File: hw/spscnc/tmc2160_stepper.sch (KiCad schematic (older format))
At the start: 65 parts, among them IC1 TMC2160-TA, Q13 KIA50N06B, Q14 KIA50N06B, Q15 KIA50N06B, Q5 KIA50N06B, Q6 KIA50N06B, Q7 KIA50N06B, Q8 KIA50N06B, Q9 KIA50N06B

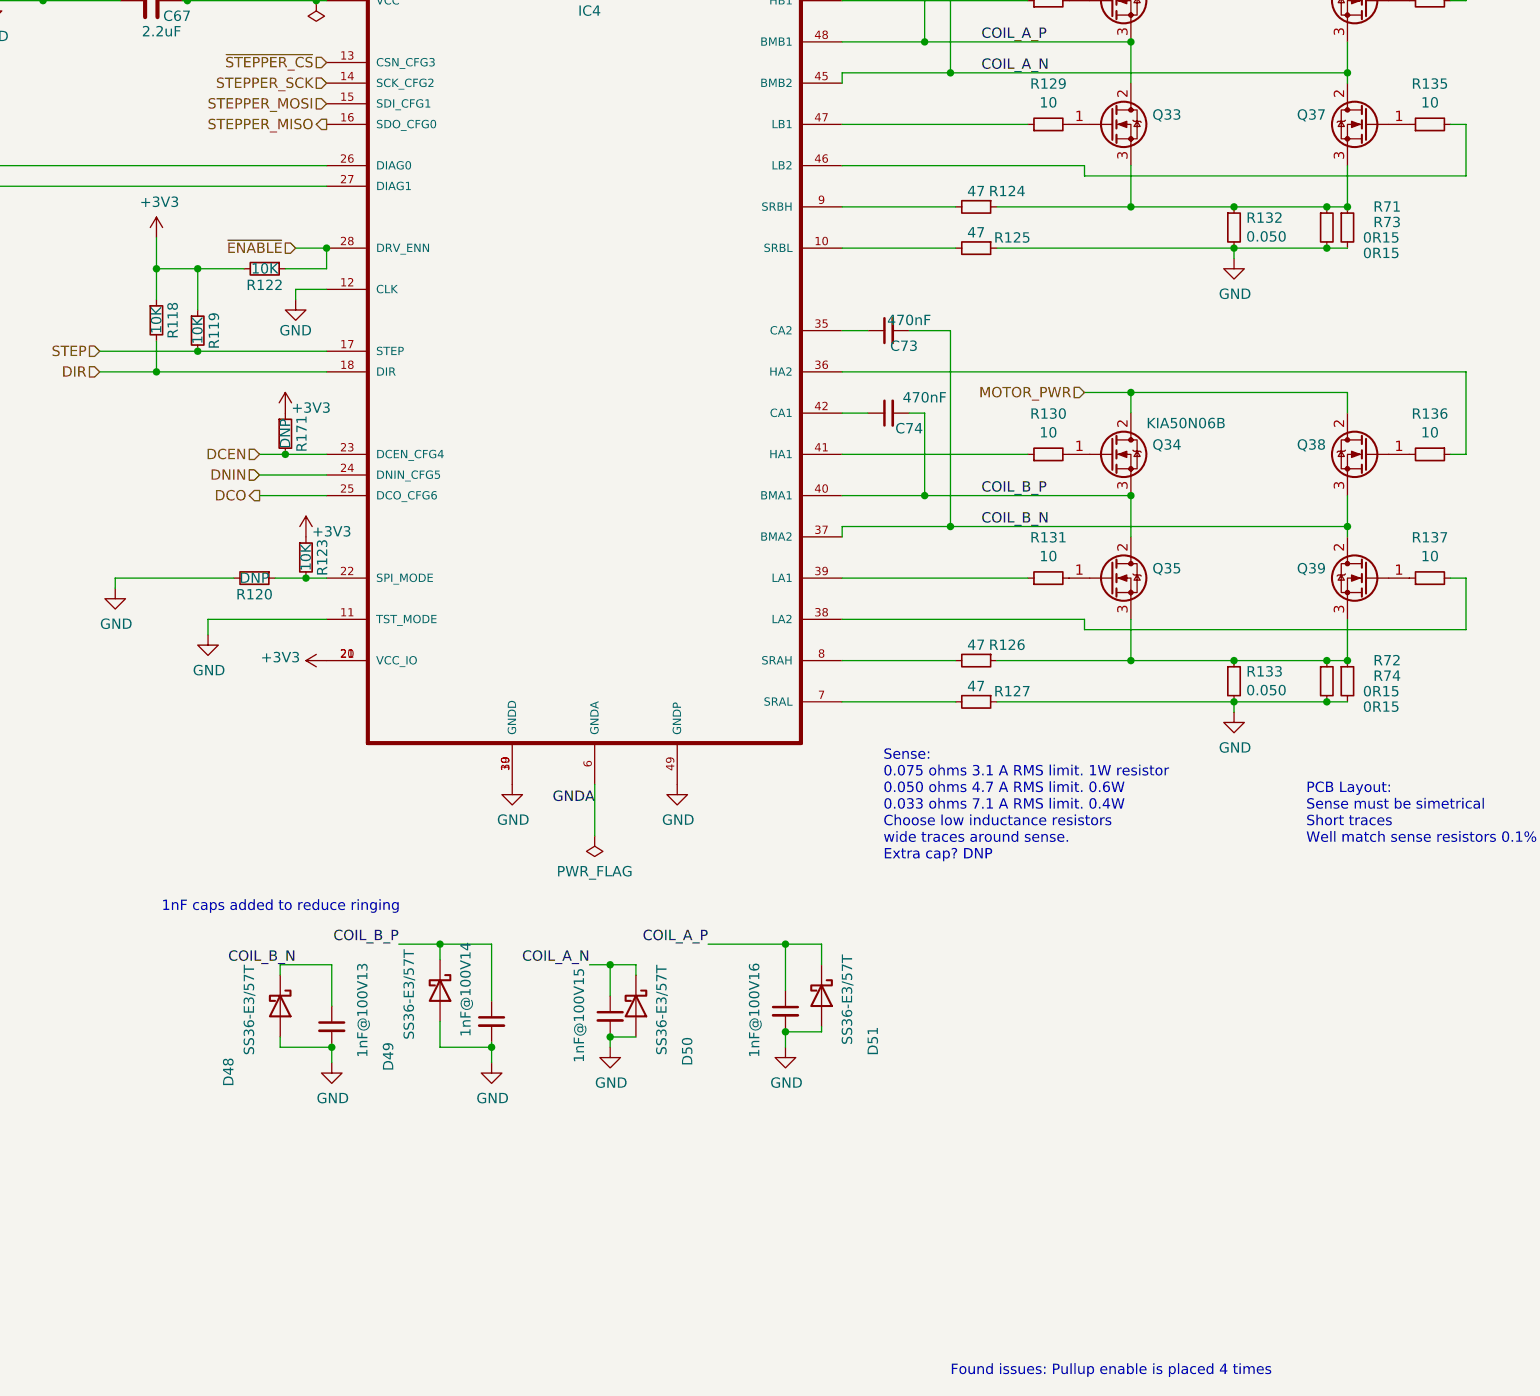
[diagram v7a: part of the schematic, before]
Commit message: Revision 1.1.0 With only critical corrections. Pending some work on the relays as that part could be remade from scratch for flexibility.
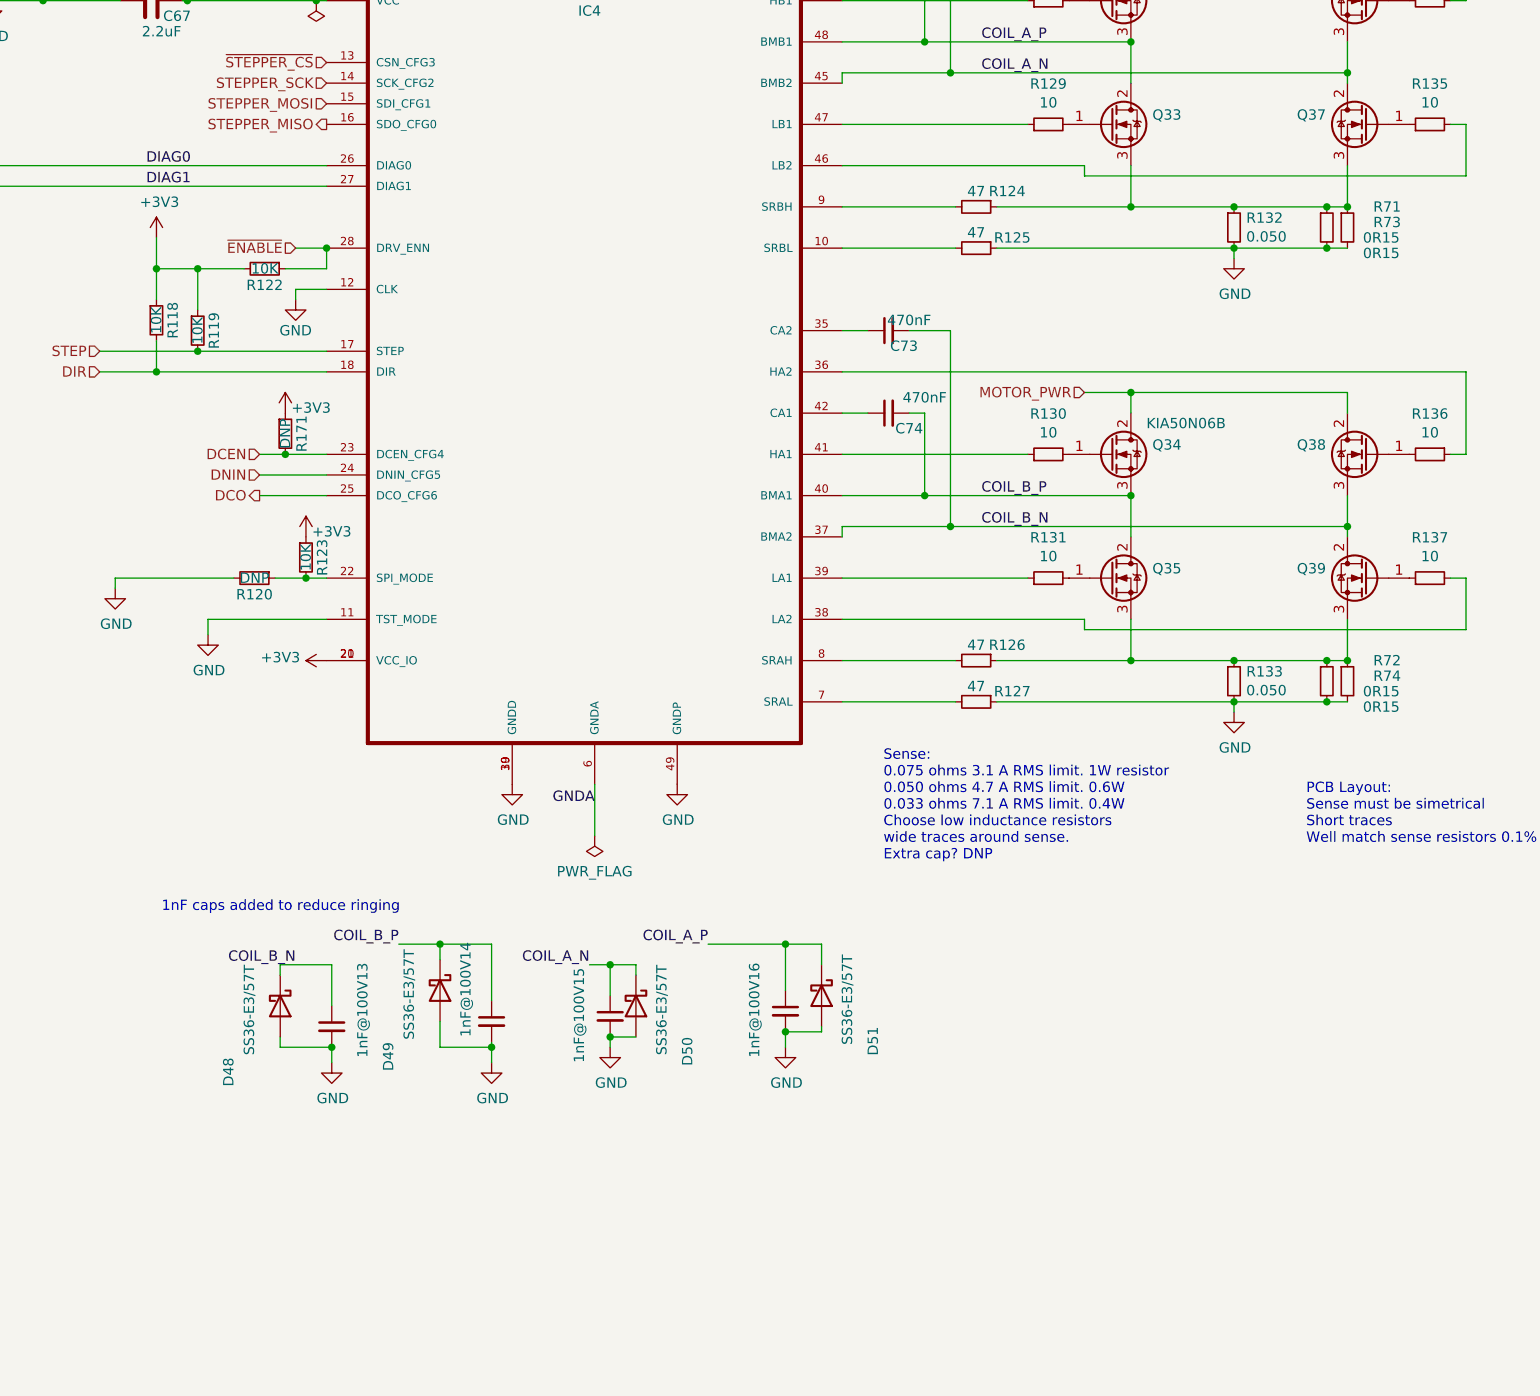
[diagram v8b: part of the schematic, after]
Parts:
- H3, H4: footprint MountingHole:MountingHole_2.2mm_M2_Pad_Via -> MountingHole:MountingHole_3.2mm_M3_Pad_Via
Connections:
- net DIAG0: now reaches D3.1 (K), IC1.26 (DIAG0)
- net DIAG1: now reaches D2.1 (K), IC1.27 (DIAG1)
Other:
- note removed: "Found issues: Pullup enable is placed 4 times"
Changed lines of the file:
@@
 Sheet 12 17
 Title "Trinamic FluidNC CNC Controller"
-Date "2022-02-12"
-Rev "1.0.1"
+Date "2022-04-29"
+Rev "1.1.0"
 Comp ""
 Comment1 ""
@@
 AR Path="/61E6E495" Ref="#PWR0103"  Part="1"
 AR Path="/6221509B/61E6E495" Ref="#PWR?"  Part="1"
-F 0 "#PWR085" H 1875 1825 50  0001 C CNN
+F 0 "#PWR065" H 1875 1825 50  0001 C CNN
 F 1 "GND" H 1880 1902 50  0000 C CNN
 F 2 "" H 1875 2075 50  0001 C CNN
@@
 AR Path="/61E77854" Ref="#PWR0104"  Part="1"
 AR Path="/6221509B/61E77854" Ref="#PWR?"  Part="1"
-F 0 "#PWR096" H 7050 800 50  0001 C CNN
+F 0 "#PWR076" H 7050 800 50  0001 C CNN
 F 1 "GND" H 7055 877 50  0000 C CNN
 F 2 "" H 7050 1050 50  0001 C CNN
@@
 AR Path="/61E77EC9" Ref="#PWR0105"  Part="1"
 AR Path="/6221509B/61E77EC9" Ref="#PWR?"  Part="1"
-F 0 "#PWR0100" H 8525 800 50  0001 C CNN
+F 0 "#PWR080" H 8525 800 50  0001 C CNN
 F 1 "GND" H 8530 877 50  0000 C CNN
 F 2 "" H 8525 1050 50  0001 C CNN
@@
 AR Path="/6203DFCF/61E7935F" Ref="#PWR091"  Part="1"
 AR Path="/6221509B/61E7935F" Ref="#PWR?"  Part="1"
-F 0 "#PWR091" H 3500 5125 50  0001 C CNN
+F 0 "#PWR071" H 3500 5125 50  0001 C CNN
 F 1 "+3V3" V 3515 5403 50  0000 L CNN
 F 2 "" H 3500 5275 50  0001 C CNN
@@
 AR Path="/61E79E80" Ref="#PWR0110"  Part="1"
 AR Path="/6221509B/61E79E80" Ref="#PWR?"  Part="1"
-F 0 "#PWR084" H 1875 1325 50  0001 C CNN
+F 0 "#PWR064" H 1875 1325 50  0001 C CNN
 F 1 "+12V" H 1890 1648 50  0000 C CNN
 F 2 "" H 1875 1475 50  0001 C CNN
@@
 AR Path="/61E86B21" Ref="#PWR0115"  Part="1"
 AR Path="/6221509B/61E86B21" Ref="#PWR?"  Part="1"
-F 0 "#PWR092" H 4400 5625 50  0001 C CNN
+F 0 "#PWR072" H 4400 5625 50  0001 C CNN
 F 1 "GND" H 4405 5702 50  0000 C CNN
 F 2 "" H 4400 5875 50  0001 C CNN
@@
 AR Path="/61E86EEA" Ref="#PWR0116"  Part="1"
 AR Path="/6221509B/61E86EEA" Ref="#PWR?"  Part="1"
-F 0 "#PWR094" H 5200 5625 50  0001 C CNN
+F 0 "#PWR074" H 5200 5625 50  0001 C CNN
 F 1 "GND" H 5205 5702 50  0000 C CNN
 F 2 "" H 5200 5875 50  0001 C CNN
@@
 AR Path="/6203DFCF/61E89FDE" Ref="#PWR087"  Part="1"
 AR Path="/6221509B/61E89FDE" Ref="#PWR?"  Part="1"
-F 0 "#PWR087" H 2675 3075 50  0001 C CNN
+F 0 "#PWR067" H 2675 3075 50  0001 C CNN
 F 1 "+3V3" H 2690 3398 50  0000 C CNN
 F 2 "" H 2675 3225 50  0001 C CNN
@@
 AR Path="/6203DFCF/61E8CEFE" Ref="#PWR089"  Part="1"
 AR Path="/6221509B/61E8CEFE" Ref="#PWR?"  Part="1"
-F 0 "#PWR089" H 3350 3275 50  0001 C CNN
+F 0 "#PWR069" H 3350 3275 50  0001 C CNN
 F 1 "GND" H 3350 3375 50  0000 C CNN
 F 2 "" H 3350 3525 50  0001 C CNN
@@
 AR Path="/6203DFCF/61EA6B53" Ref="#PWR090"  Part="1"
 AR Path="/6221509B/61EA6B53" Ref="#PWR?"  Part="1"
-F 0 "#PWR090" H 3400 4525 50  0001 C CNN
+F 0 "#PWR070" H 3400 4525 50  0001 C CNN
 F 1 "+3V3" H 3525 4700 50  0000 C CNN
 F 2 "" H 3400 4675 50  0001 C CNN
@@
 AR Path="/61ECB3CC" Ref="#PWR0121"  Part="1"
 AR Path="/6221509B/61ECB3CC" Ref="#PWR?"  Part="1"
-F 0 "#PWR099" H 8075 800 50  0001 C CNN
+F 0 "#PWR079" H 8075 800 50  0001 C CNN
 F 1 "GND" H 8080 877 50  0000 C CNN
 F 2 "" H 8075 1050 50  0001 C CNN
@@
 AR Path="/61F1EBF7" Ref="#PWR0122"  Part="1"
 AR Path="/6221509B/61F1EBF7" Ref="#PWR?"  Part="1"
-F 0 "#PWR097" H 7900 3075 50  0001 C CNN
+F 0 "#PWR077" H 7900 3075 50  0001 C CNN
 F 1 "GND" H 7905 3152 50  0000 C CNN
 F 2 "" H 7900 3325 50  0001 C CNN
@@
 AR Path="/61F26F6F" Ref="#PWR0123"  Part="1"
 AR Path="/6221509B/61F26F6F" Ref="#PWR?"  Part="1"
-F 0 "#PWR088" H 2925 4900 50  0001 C CNN
+F 0 "#PWR068" H 2925 4900 50  0001 C CNN
 F 1 "GND" H 2930 4977 50  0000 C CNN
 F 2 "" H 2925 5150 50  0001 C CNN
@@
 AR Path="/61F3F591" Ref="#PWR0124"  Part="1"
 AR Path="/6221509B/61F3F591" Ref="#PWR?"  Part="1"
-F 0 "#PWR086" H 2475 4675 50  0001 C CNN
+F 0 "#PWR066" H 2475 4675 50  0001 C CNN
 F 1 "GND" H 2480 4752 50  0000 C CNN
 F 2 "" H 2475 4925 50  0001 C CNN
@@
 F 0 "H7" H 10575 5674 50  0000 L CNN
 F 1 "MountingHole_Pad" H 10575 5583 50  0001 L CNN
-F 2 "MountingHole:MountingHole_2.2mm_M2_Pad_Via" H 10475 5625 50  0001 C CNN
+F 2 "MountingHole:MountingHole_3.2mm_M3_Pad_Via" H 10475 5625 50  0001 C CNN
 F 3 "~" H 10475 5625 50  0001 C CNN
 F 4 "DNP003" H 10475 5625 50  0001 C CNN "jlcpcb"
@@
 AR Path="/61F4F366" Ref="#PWR0125"  Part="1"
 AR Path="/6221509B/61F4F366" Ref="#PWR?"  Part="1"
-F 0 "#PWR095" H 10475 5475 50  0001 C CNN
+F 0 "#PWR075" H 10475 5475 50  0001 C CNN
 F 1 "GND" H 10480 5552 50  0000 C CNN
 F 2 "" H 10475 5725 50  0001 C CNN
@@
 AR Path="/61F62E48" Ref="#PWR0126"  Part="1"
 AR Path="/6221509B/61F62E48" Ref="#PWR?"  Part="1"
-F 0 "#PWR0120" H 9075 800 50  0001 C CNN
+F 0 "#PWR081" H 9075 800 50  0001 C CNN
 F 1 "GND" H 9080 877 50  0000 C CNN
 F 2 "" H 9075 1050 50  0001 C CNN
@@
 AR Path="/61F7F4E7" Ref="#PWR0127"  Part="1"
 AR Path="/6221509B/61F7F4E7" Ref="#PWR?"  Part="1"
-F 0 "#PWR098" H 7900 5275 50  0001 C CNN
+F 0 "#PWR078" H 7900 5275 50  0001 C CNN
 F 1 "GND" H 7905 5352 50  0000 C CNN
 F 2 "" H 7900 5525 50  0001 C CNN
@@
 AR Path="/620590A8" Ref="#FLG0110"  Part="1"
 AR Path="/6221509B/620590A8" Ref="#FLG?"  Part="1"
-F 0 "#FLG0113" H 3450 2150 50  0001 C CNN
+F 0 "#FLG0112" H 3450 2150 50  0001 C CNN
 F 1 "PWR_FLAG" H 3450 2248 50  0001 C CNN
 F 2 "" H 3450 2075 50  0001 C CNN
@@
 F 0 "H10" H 10225 5674 50  0000 L CNN
 F 1 "MountingHole_Pad" H 10225 5583 50  0001 L CNN
-F 2 "MountingHole:MountingHole_2.2mm_M2_Pad_Via" H 10125 5625 50  0001 C CNN
+F 2 "MountingHole:MountingHole_3.2mm_M3_Pad_Via" H 10125 5625 50  0001 C CNN
 F 3 "~" H 10125 5625 50  0001 C CNN
 F 4 "DNP003" H 10125 5625 50  0001 C CNN "jlcpcb"
@@
 AR Path="/61FC2A3D" Ref="#PWR03"  Part="1"
 AR Path="/6221509B/61FC2A3D" Ref="#PWR?"  Part="1"
-F 0 "#PWR037" H 10125 5475 50  0001 C CNN
+F 0 "#PWR06" H 10125 5475 50  0001 C CNN
 F 1 "GND" H 10130 5552 50  0000 C CNN
 F 2 "" H 10125 5725 50  0001 C CNN
@@
 AR Path="/6203DFCF/61F301A3" Ref="#PWR0239"  Part="1"
 AR Path="/6221509B/61F301A3" Ref="#PWR?"  Part="1"
-F 0 "#PWR0239" H 3300 3925 50  0001 C CNN
+F 0 "#PWR0238" H 3300 3925 50  0001 C CNN
 F 1 "+3V3" H 3425 4100 50  0000 C CNN
 F 2 "" H 3300 4075 50  0001 C CNN
@@
 AR Path="/6203DFCF/61F599E0" Ref="#PWR0244"  Part="1"
 AR Path="/6221509B/61F599E0" Ref="#PWR?"  Part="1"
-F 0 "#PWR0244" H 1425 2125 50  0001 C CNN
+F 0 "#PWR0242" H 1425 2125 50  0001 C CNN
 F 1 "+3V3" H 1440 2448 50  0000 C CNN
 F 2 "" H 1425 2275 50  0001 C CNN
@@
 AR Path="/6203DFCF/61F5A3EC" Ref="#PWR0245"  Part="1"
 AR Path="/6221509B/61F5A3EC" Ref="#PWR?"  Part="1"
-F 0 "#PWR0245" H 1050 2200 50  0001 C CNN
+F 0 "#PWR0243" H 1050 2200 50  0001 C CNN
 F 1 "+3V3" H 1065 2523 50  0000 C CNN
 F 2 "" H 1050 2350 50  0001 C CNN
@@
 AR Path="/61FAA995" Ref="#PWR0247"  Part="1"
 AR Path="/6221509B/61FAA995" Ref="#PWR?"  Part="1"
-F 0 "#PWR0259" H 3525 6975 50  0001 C CNN
+F 0 "#PWR0255" H 3525 6975 50  0001 C CNN
 F 1 "GND" H 3530 7052 50  0000 C CNN
 F 2 "" H 3525 7225 50  0001 C CNN
@@
 AR Path="/61FAED05" Ref="#PWR0248"  Part="1"
 AR Path="/6221509B/61FAED05" Ref="#PWR?"  Part="1"
-F 0 "#PWR0260" H 4300 6975 50  0001 C CNN
+F 0 "#PWR0256" H 4300 6975 50  0001 C CNN
 F 1 "GND" H 4305 7052 50  0000 C CNN
 F 2 "" H 4300 7225 50  0001 C CNN
@@
 AR Path="/61FB6882" Ref="#PWR0249"  Part="1"
 AR Path="/6221509B/61FB6882" Ref="#PWR?"  Part="1"
-F 0 "#PWR0261" H 4875 6900 50  0001 C CNN
+F 0 "#PWR0257" H 4875 6900 50  0001 C CNN
 F 1 "GND" H 4880 6977 50  0000 C CNN
 F 2 "" H 4875 7150 50  0001 C CNN
@@
 AR Path="/61FBE4C1" Ref="#PWR0250"  Part="1"
 AR Path="/6221509B/61FBE4C1" Ref="#PWR?"  Part="1"
-F 0 "#PWR0262" H 5725 6900 50  0001 C CNN
+F 0 "#PWR0258" H 5725 6900 50  0001 C CNN
 F 1 "GND" H 5730 6977 50  0000 C CNN
 F 2 "" H 5725 7150 50  0001 C CNN
@@
 AR Path="/61F8983B" Ref="#FLG0104"  Part="1"
 AR Path="/6221509B/61F8983B" Ref="#FLG?"  Part="1"
-F 0 "#FLG0114" H 4800 6200 50  0001 C CNN
+F 0 "#FLG0115" H 4800 6200 50  0001 C CNN
 F 1 "PWR_FLAG" H 4800 6298 50  0000 C CNN
 F 2 "" H 4800 6125 50  0001 C CNN
@@
 Wire Wire Line
 	4800 6125 4800 5875
-Text Notes 6525 8750 0    50   ~ 0
-Found issues: Pullup enable is placed 4 times
+Text Label 2625 2875 0    50   ~ 0
+DIAG0
+Text Label 2625 2975 0    50   ~ 0
+DIAG1
 $EndSCHEMATC
